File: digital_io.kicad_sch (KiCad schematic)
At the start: 28 parts, among them CN3 KF250-3.5-2P-2, CN4 KF250-3.5-2P-2, Q2 BC817, Q3 BC817, Q4 BC817, Q5 BC817

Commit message: Checkpoint: RA5 base board finished, M.2 shield interconnect defined
Base board (ra5_2022):
- Finalize component placement on ra5_2022.kicad_pcb; next step is routing
- Add STM8S003F3P to bridge the 2 digital inputs / 2 digital outputs onto
  the shared I2C bus (alongside the ADS1115), freeing up M.2 pins
- Wire J1 (M.2 Key-E) to a custom, non-spec-compliant 3.3V pinout: I2C
  (SDA/SCL/ALERT#) on the native pins, M90E32AS SPI reusing the SD/SDIO
  "SPI mode" pin convention (SCLK/MOSI/MISO/CS), PM0/PM1 on VENDOR_DEFINED
  pins, USB-C passthrough, full GND/VDD
- Fix AS0BC21-S40BE-7H footprint: pads 76/77 (shield/ground tabs, not part
  of the 75-pin M.2 spec) remapped onto the GND pin instead of dangling
- Swap the buck inductor (L2) for SLW5040S100MST (C182189): same 10uH,
  lower DCR, 5x5mm footprint to clear a routing constraint
- Remove the unused "Production" KiCad Design Variant and align the
  remaining "Develop" variant's footprints with the defaults -- a
  variant/default footprint mismatch was causing Update PCB from Schematic
  to silently duplicate footprints on every sync
- Clean up 10 further orphaned duplicate footprints left on the PCB from
  earlier design revisions (R11, R12, C14, C16, C17, C18, C29, C31, C32, C35)
- Fix 3D model paths across the shared library to use the RA5_2022_LIB
  environment variable instead of ${KIPRJMOD}, so previews resolve
  correctly from sibling projects too

New sibling project (ra5_shield_modem/):
- MCU + LTE modem card, built to the M.2 Key-E mechanical form factor to
  plug into the base board's J1
- Share the ra5_2022 parts library via sym-lib-table/fp-lib-table
- Add the timonsku/M.2-Card-Footprints submodule as a card-edge template

Co-Authored-By: Claude Sonnet 5 <noreply@anthropic.com>
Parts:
- D12: renamed from D14; footprint Diode_THT:D_DO-41_SOD81_P10.16mm_Horizontal -> Diode_SMD:D_SOD-123F
- D16: footprint Diode_THT:D_DO-41_SOD81_P10.16mm_Horizontal -> Diode_SMD:D_SOD-123F
- renumbered D9 to D10, D10 to D11, D15 to D13, D11 to D14, D12 to D15, D13 to D9, Q4 to Q2, Q2 to Q3, Q5 to Q4, Q3 to Q5, R62 to R60, R70 to R61, R63 to R62, R71 to R63, R72 to R64, R64 to R65, R65 to R66, R66 to R67, R73 to R68, R67 to R69, R74 to R70, R75 to R71, R68 to R72, R69 to R73
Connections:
- net DI1: now also CN3.2; no longer CN3.1
- net DI2: now also CN3.1; no longer CN3.2
- net DO1: now also CN4.2; no longer CN4.1
- net DO2: now also CN4.1; no longer CN4.2

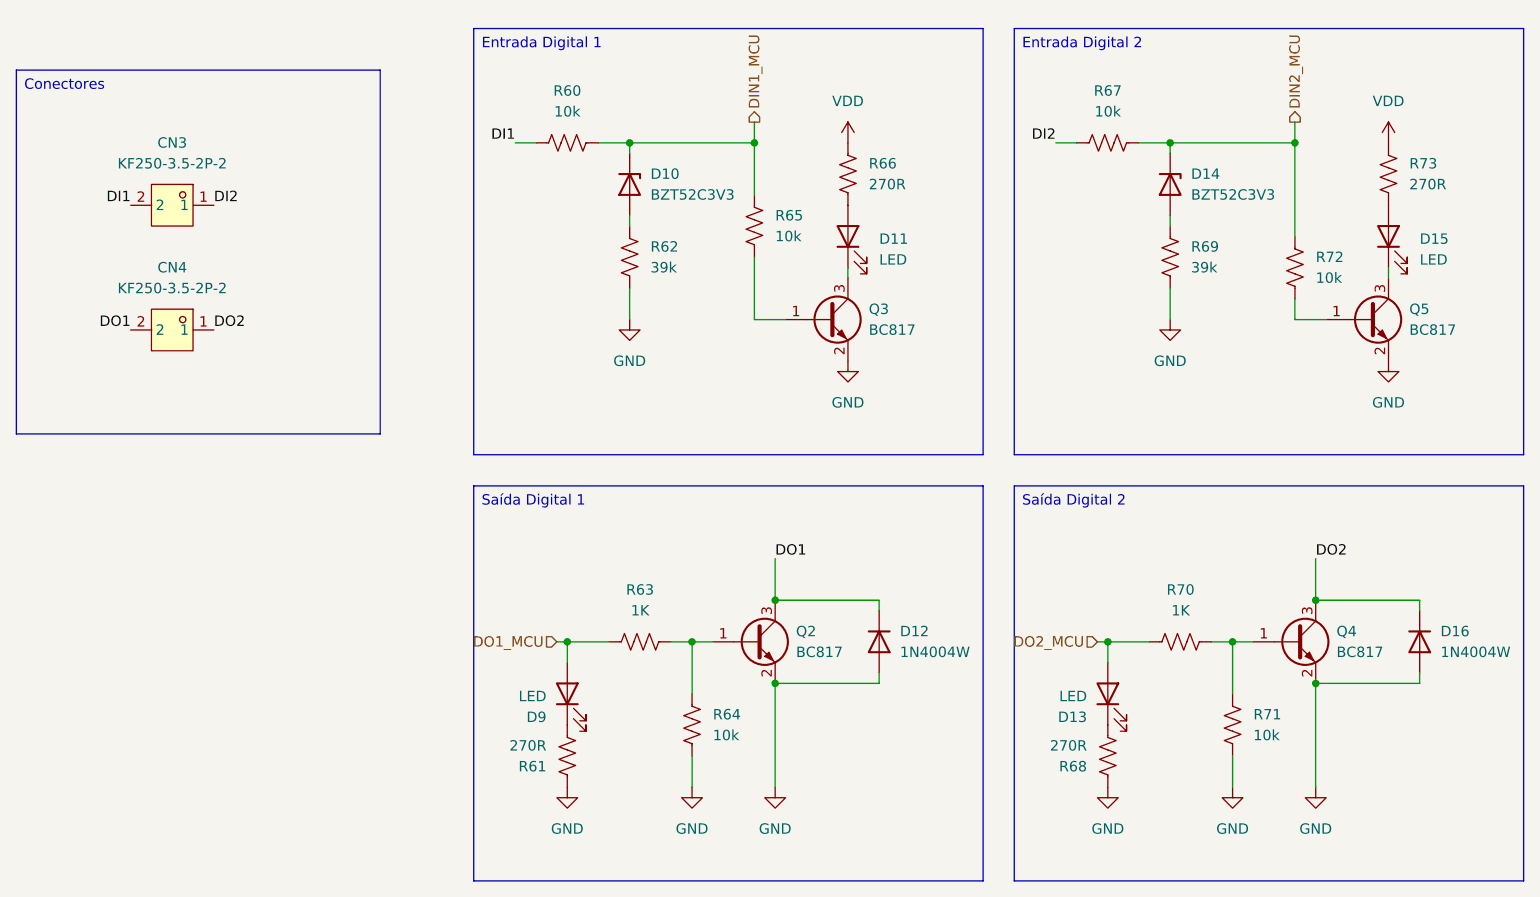
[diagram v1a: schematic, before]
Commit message: Migra componentes das bibliotecas LCSC locais para pecas JLCPCB
Troca os part numbers para casar com o estoque da JLCPCB e com o
catalogo PCBA Basic, eliminando a biblioteca local que era importada
via easyeda2kicad.

- Remove libraries/ (simbolos, footprints e modelos 3D importados) e o
  script import_lcsc_component.sh
- Adiciona o plugin JLCPCB (jlcpcb/project.db) e os scripts auxiliares
  fix_jlcpcb_tools_deps.sh e generate_ibom.sh
- Atualiza as cinco folhas do esquematico, o PCB e as regras de projeto

O PCB fica em estado intermediario: os componentes novos ainda precisam
ser reposicionados e as trilhas refeitas.

Co-Authored-By: Claude Opus 5 (1M context) <noreply@anthropic.com>
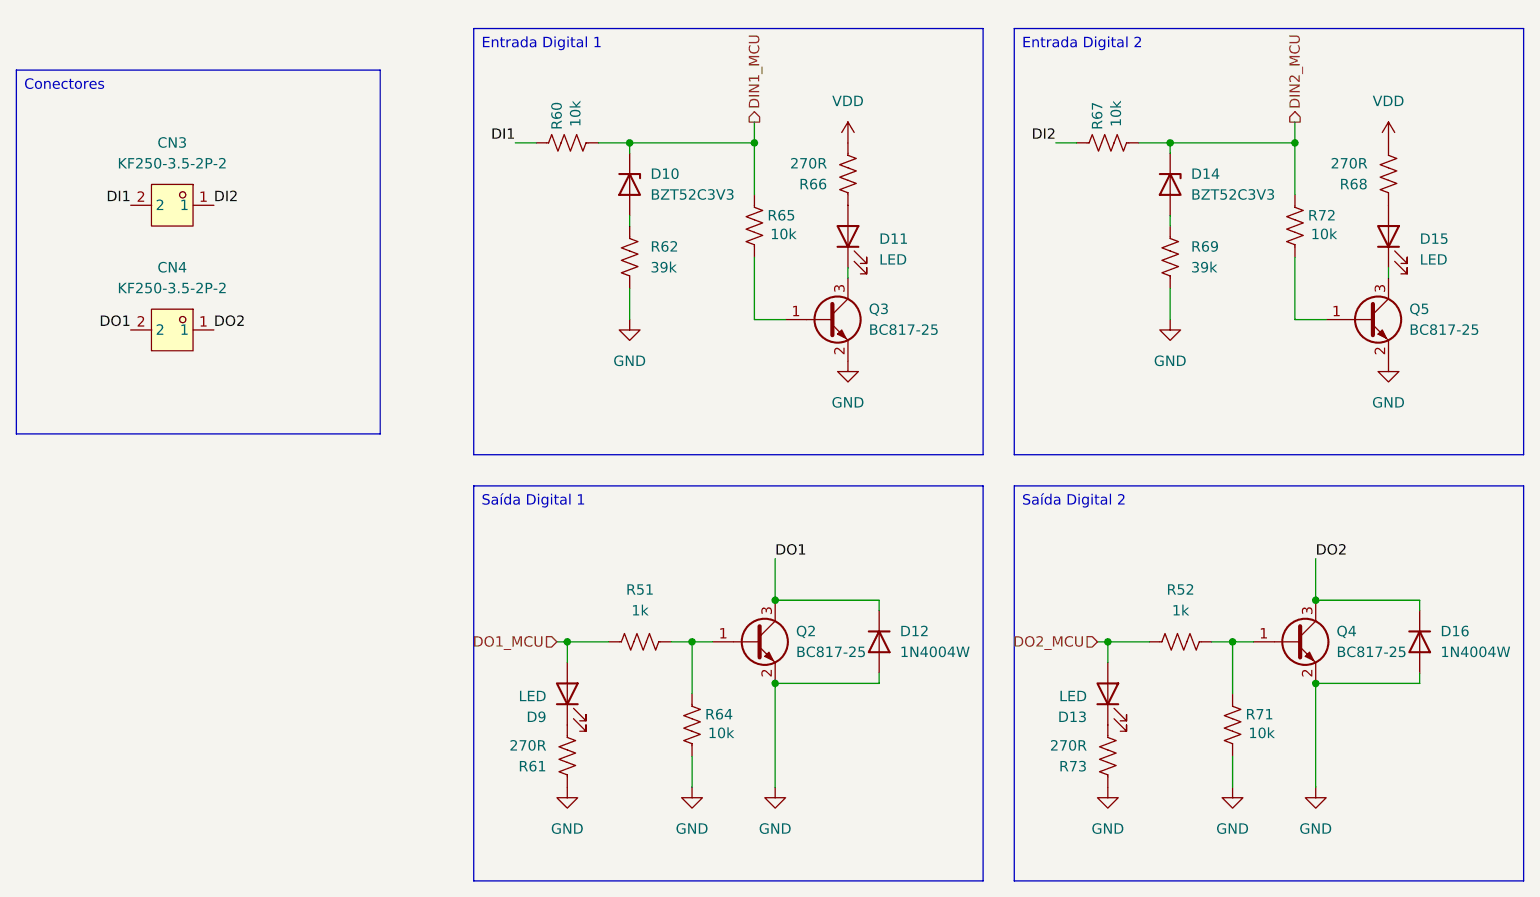
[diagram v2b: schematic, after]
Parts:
- removed R63, R70: 1K, Resistor_SMD:R_0603_1608Metric, symbol Device:R_US
- added R51, R52: 1k, Resistor_SMD:R_0402_1005Metric, symbol Device:R_US
- CN3: JLCPCB Part # (none) -> C475163; LCSC Part # C475163 -> (none)
- CN4: JLCPCB Part # (none) -> C475163; LCSC Part C475163 -> (none); LCSC Part # C475163 -> (none)
- D10, D14: JLCPCB Part # (none) -> C216707; LCSC Part # C216707 -> (none)
- D11, D13, D15, D9: JLCPCB Part # (none) -> C19171391; LCSC Part # C19171391 -> (none)
- D12, D16: JLCPCB Part # (none) -> C162734; LCSC Part # C162734 -> (none)
- Q2, Q3, Q4, Q5: value BC817 -> BC817-25; JLCPCB Part # (none) -> C20069154; LCSC Part # C549433 -> (none); MPN BC817-25,235 -> BC817-25
- R60, R64, R65, R67, R71, R72: footprint Resistor_SMD:R_0805_2012Metric -> Resistor_SMD:R_0402_1005Metric; JLCPCB Part # (none) -> C25744; LCSC Part # C431835 -> (none); MPN MR08X1002FTL -> 0402WGF1002TCE
- R61, R66, R68, R73: JLCPCB Part # (none) -> C22966; LCSC Part # C2105700 -> (none); MPN RCS0603270RFKEA -> 0603WAF2700T5E
- R62, R69: JLCPCB Part # (none) -> C23153; LCSC Part # C54921034 -> (none); MPN HRC0603J393 ENTN -> 0603WAF3902T5E
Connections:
- net DI1: now also R60.2; no longer R60.1
- net DI2: now also R67.2; no longer R67.1
- net DIN1_MCU: now also R60.1; no longer R60.2
- net DIN2_MCU: now also R67.1; no longer R67.2
- net DO1_MCU: now also R51.1
- net DO2_MCU: now also R52.1
- net GND: now also R73.2; no longer R68.2
- net VDD: now also R66.1, R68.1; no longer R66.2, R73.2
- net at D15.2 (A): now also R68.2; no longer R73.1
- net at D11.2 (A): now also R66.2; no longer R66.1
- net at Q4.1 (B), R71.2: now also R52.2
- net at Q2.1 (B), R64.2: now also R51.2
- net at D13.1 (K): now also R73.1; no longer R68.1
